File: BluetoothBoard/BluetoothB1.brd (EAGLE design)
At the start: 160 x 100 mm, 5 parts, among them U1 SPBTLE-RF

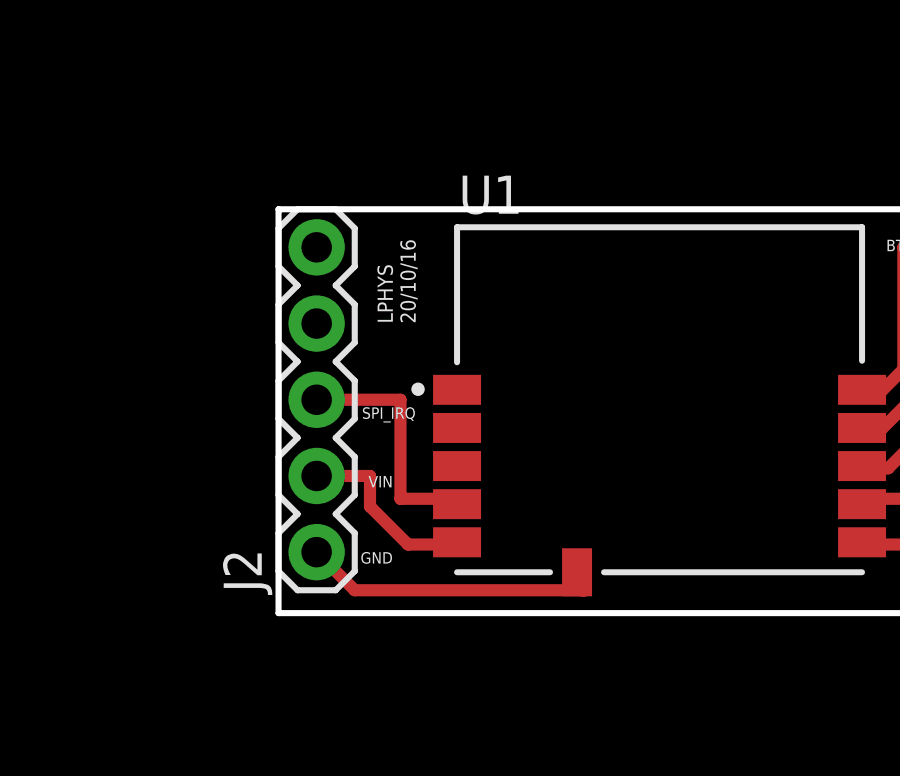
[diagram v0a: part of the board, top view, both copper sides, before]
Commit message: created complete LSM6DS3 implementation + configured Bluetooth to be printed
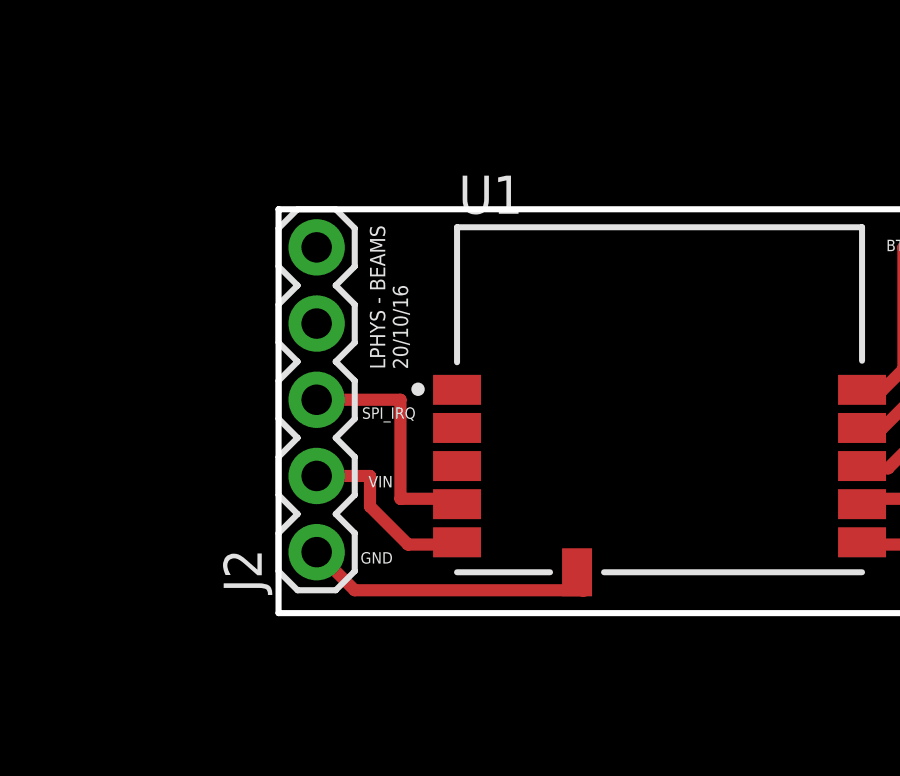
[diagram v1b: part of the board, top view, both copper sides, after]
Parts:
- removed FRAME1: FRAME-LETTER, SparkFun-Aesthetics:CREATIVE_COMMONS
- removed LOGO1: BREADBOARD_PATTERN, SparkFun-Aesthetics:BREADBOARD_SPACING
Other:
- board text added: "LPHYS - BEAMS 20/10/16"
- board text removed: "LPHYS 20/10/16"
